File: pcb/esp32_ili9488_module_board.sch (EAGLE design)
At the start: 20 parts, among them U1 ILI9488 module, U2 ESP-WROOM/WROVER-32, U3 APK2112K-3.3TRG1, X1 HEADER-FTDI232, X2 USB-MICRO-B-FCI, X3 BOOT, X4 RESET, X5 QWIIC

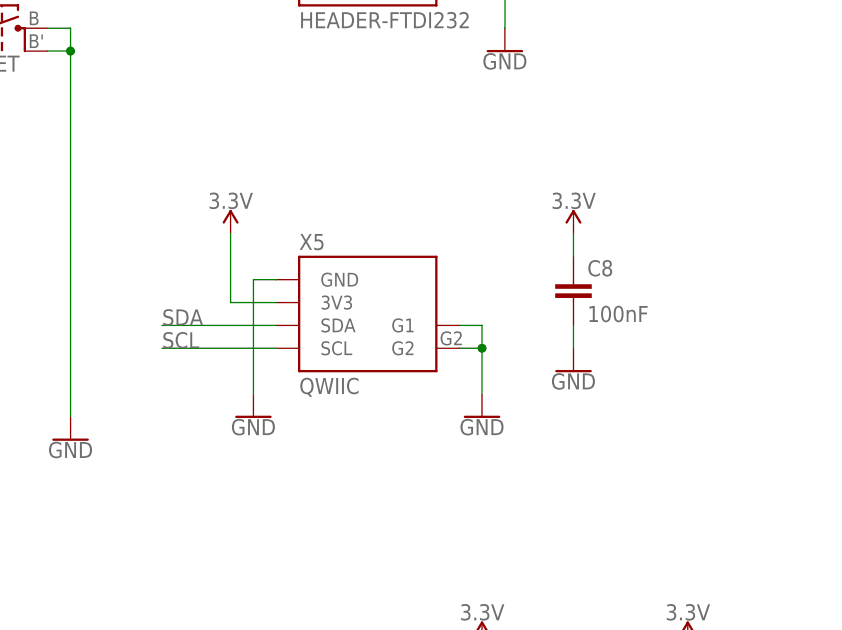
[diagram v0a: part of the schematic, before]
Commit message: Add I2C pullups
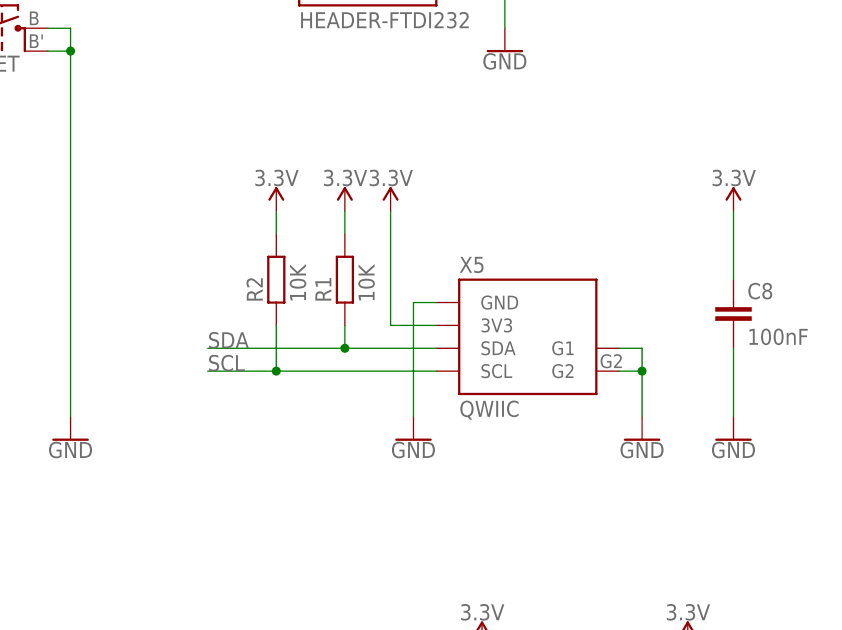
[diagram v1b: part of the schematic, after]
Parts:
- added R1, R2: 10K, M2M-Passives:RESISTOR0603
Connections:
- net 3.3V: now also R1.2, R2.2
- net SCL: now also R2.1
- net SDA: now also R1.1
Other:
- moved on the sheet: C8, X5
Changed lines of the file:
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@@
 <part name="SUPPLY13" library="M2M-Power" deviceset="3.3V" device=""/>
 <part name="GND20" library="M2M-Power" deviceset="GND" device=""/>
+<part name="R1" library="M2M-Passives" deviceset="RESISTOR" device="0603" value="10K"/>
+<part name="R2" library="M2M-Passives" deviceset="RESISTOR" device="0603" value="10K"/>
+<part name="SUPPLY14" library="M2M-Power" deviceset="3.3V" device=""/>
+<part name="SUPPLY15" library="M2M-Power" deviceset="3.3V" device=""/>
 </parts>
 <sheets>
@@
 <attribute name="VALUE" x="12.7" y="144.526" size="1.778" layer="96" align="top-center"/>
 </instance>
-<instance part="X5" gate="G$1" x="200.66" y="106.68" smashed="yes">
-<attribute name="NAME" x="193.04" y="115.062" size="1.778" layer="95"/>
-<attribute name="VALUE" x="193.04" y="99.06" size="1.778" layer="96"/>
-</instance>
-<instance part="GND17" gate="1" x="213.36" y="96.52" smashed="yes">
-<attribute name="VALUE" x="213.36" y="96.266" size="1.778" layer="96" align="top-center"/>
-</instance>
-<instance part="GND18" gate="1" x="187.96" y="96.52" smashed="yes">
-<attribute name="VALUE" x="187.96" y="96.266" size="1.778" layer="96" align="top-center"/>
-</instance>
-<instance part="SUPPLY11" gate="G$1" x="185.42" y="116.84" smashed="yes">
-<attribute name="VALUE" x="185.42" y="119.634" size="1.778" layer="96" align="bottom-center"/>
+<instance part="X5" gate="G$1" x="218.44" y="104.14" smashed="yes">
+<attribute name="NAME" x="210.82" y="112.522" size="1.778" layer="95"/>
+<attribute name="VALUE" x="210.82" y="96.52" size="1.778" layer="96"/>
+</instance>
+<instance part="GND17" gate="1" x="231.14" y="93.98" smashed="yes">
+<attribute name="VALUE" x="231.14" y="93.726" size="1.778" layer="96" align="top-center"/>
+</instance>
+<instance part="GND18" gate="1" x="205.74" y="93.98" smashed="yes">
+<attribute name="VALUE" x="205.74" y="93.726" size="1.778" layer="96" align="top-center"/>
+</instance>
+<instance part="SUPPLY11" gate="G$1" x="203.2" y="119.38" smashed="yes">
+<attribute name="VALUE" x="203.2" y="122.174" size="1.778" layer="96" align="bottom-center"/>
 </instance>
 <instance part="C7" gate="G$1" x="236.22" y="66.04" smashed="yes">
@@
 <attribute name="VALUE" x="236.22" y="55.626" size="1.778" layer="96" align="top-center"/>
 </instance>
-<instance part="C8" gate="G$1" x="223.52" y="111.76" smashed="yes">
-<attribute name="NAME" x="225.044" y="112.141" size="1.778" layer="95"/>
-<attribute name="VALUE" x="225.044" y="107.061" size="1.778" layer="96"/>
-</instance>
-<instance part="SUPPLY13" gate="G$1" x="223.52" y="116.84" smashed="yes">
-<attribute name="VALUE" x="223.52" y="119.634" size="1.778" layer="96" align="bottom-center"/>
-</instance>
-<instance part="GND20" gate="1" x="223.52" y="101.6" smashed="yes">
-<attribute name="VALUE" x="223.52" y="101.346" size="1.778" layer="96" align="top-center"/>
+<instance part="C8" gate="G$1" x="241.3" y="109.22" smashed="yes">
+<attribute name="NAME" x="242.824" y="109.601" size="1.778" layer="95"/>
+<attribute name="VALUE" x="242.824" y="104.521" size="1.778" layer="96"/>
+</instance>
+<instance part="SUPPLY13" gate="G$1" x="241.3" y="119.38" smashed="yes">
+<attribute name="VALUE" x="241.3" y="122.174" size="1.778" layer="96" align="bottom-center"/>
+</instance>
+<instance part="GND20" gate="1" x="241.3" y="93.98" smashed="yes">
+<attribute name="VALUE" x="241.3" y="93.726" size="1.778" layer="96" align="top-center"/>
+</instance>
+<instance part="R1" gate="G$1" x="198.12" y="111.76" smashed="yes" rot="R90">
+<attribute name="NAME" x="196.6214" y="109.22" size="1.778" layer="95" rot="R90"/>
+<attribute name="VALUE" x="201.422" y="109.22" size="1.778" layer="96" rot="R90"/>
+</instance>
+<instance part="R2" gate="G$1" x="190.5" y="111.76" smashed="yes" rot="R90">
+<attribute name="NAME" x="189.0014" y="109.22" size="1.778" layer="95" rot="R90"/>
+<attribute name="VALUE" x="193.802" y="109.22" size="1.778" layer="96" rot="R90"/>
+</instance>
+<instance part="SUPPLY14" gate="G$1" x="198.12" y="119.38" smashed="yes">
+<attribute name="VALUE" x="198.12" y="122.174" size="1.778" layer="96" align="bottom-center"/>
+</instance>
+<instance part="SUPPLY15" gate="G$1" x="190.5" y="119.38" smashed="yes">
+<attribute name="VALUE" x="190.5" y="122.174" size="1.778" layer="96" align="bottom-center"/>
 </instance>
 </instances>
@@
 <pinref part="GND18" gate="1" pin="GND"/>
 <pinref part="X5" gate="G$1" pin="GND"/>
-<wire x1="187.96" y1="99.06" x2="187.96" y2="111.76" width="0.1524" layer="91"/>
-<wire x1="187.96" y1="111.76" x2="190.5" y2="111.76" width="0.1524" layer="91"/>
+<wire x1="205.74" y1="96.52" x2="205.74" y2="109.22" width="0.1524" layer="91"/>
+<wire x1="205.74" y1="109.22" x2="208.28" y2="109.22" width="0.1524" layer="91"/>
 </segment>
 <segment>
 <pinref part="GND17" gate="1" pin="GND"/>
 <pinref part="X5" gate="G$1" pin="G1"/>
-<wire x1="213.36" y1="99.06" x2="213.36" y2="104.14" width="0.1524" layer="91"/>
-<wire x1="213.36" y1="104.14" x2="213.36" y2="106.68" width="0.1524" layer="91"/>
-<wire x1="213.36" y1="106.68" x2="210.82" y2="106.68" width="0.1524" layer="91"/>
+<wire x1="231.14" y1="96.52" x2="231.14" y2="101.6" width="0.1524" layer="91"/>
+<wire x1="231.14" y1="101.6" x2="231.14" y2="104.14" width="0.1524" layer="91"/>
+<wire x1="231.14" y1="104.14" x2="228.6" y2="104.14" width="0.1524" layer="91"/>
 <pinref part="X5" gate="G$1" pin="G2"/>
-<wire x1="210.82" y1="104.14" x2="213.36" y2="104.14" width="0.1524" layer="91"/>
-<junction x="213.36" y="104.14"/>
+<wire x1="228.6" y1="101.6" x2="231.14" y2="101.6" width="0.1524" layer="91"/>
+<junction x="231.14" y="101.6"/>
 </segment>
 <segment>
@@
 <pinref part="C8" gate="G$1" pin="2"/>
 <pinref part="GND20" gate="1" pin="GND"/>
-<wire x1="223.52" y1="106.68" x2="223.52" y2="104.14" width="0.1524" layer="91"/>
+<wire x1="241.3" y1="104.14" x2="241.3" y2="96.52" width="0.1524" layer="91"/>
 </segment>
 </net>
@@
 <segment>
 <pinref part="X5" gate="G$1" pin="3V3"/>
-<wire x1="190.5" y1="109.22" x2="185.42" y2="109.22" width="0.1524" layer="91"/>
+<wire x1="208.28" y1="106.68" x2="203.2" y2="106.68" width="0.1524" layer="91"/>
 <pinref part="SUPPLY11" gate="G$1" pin="3.3V"/>
-<wire x1="185.42" y1="109.22" x2="185.42" y2="116.84" width="0.1524" layer="91"/>
+<wire x1="203.2" y1="106.68" x2="203.2" y2="119.38" width="0.1524" layer="91"/>
 </segment>
 <segment>
@@
 <pinref part="SUPPLY13" gate="G$1" pin="3.3V"/>
 <pinref part="C8" gate="G$1" pin="1"/>
-<wire x1="223.52" y1="116.84" x2="223.52" y2="114.3" width="0.1524" layer="91"/>
+<wire x1="241.3" y1="119.38" x2="241.3" y2="111.76" width="0.1524" layer="91"/>
+</segment>
+<segment>
+<pinref part="SUPPLY15" gate="G$1" pin="3.3V"/>
+<pinref part="R2" gate="G$1" pin="2"/>
+<wire x1="190.5" y1="119.38" x2="190.5" y2="116.84" width="0.1524" layer="91"/>
+</segment>
+<segment>
+<pinref part="SUPPLY14" gate="G$1" pin="3.3V"/>
+<pinref part="R1" gate="G$1" pin="2"/>
+<wire x1="198.12" y1="119.38" x2="198.12" y2="116.84" width="0.1524" layer="91"/>
 </segment>
 </net>
@@
 <segment>
 <pinref part="X5" gate="G$1" pin="SDA"/>
-<wire x1="190.5" y1="106.68" x2="177.8" y2="106.68" width="0.1524" layer="91"/>
-<label x="177.8" y="106.68" size="1.778" layer="95"/>
+<wire x1="208.28" y1="104.14" x2="198.12" y2="104.14" width="0.1524" layer="91"/>
+<label x="182.88" y="104.14" size="1.778" layer="95"/>
+<pinref part="R1" gate="G$1" pin="1"/>
+<wire x1="198.12" y1="104.14" x2="182.88" y2="104.14" width="0.1524" layer="91"/>
+<wire x1="198.12" y1="106.68" x2="198.12" y2="104.14" width="0.1524" layer="91"/>
+<junction x="198.12" y="104.14"/>
 </segment>
 <segment>
@@
 <segment>
 <pinref part="X5" gate="G$1" pin="SCL"/>
-<wire x1="190.5" y1="104.14" x2="177.8" y2="104.14" width="0.1524" layer="91"/>
-<label x="177.8" y="104.14" size="1.778" layer="95"/>
-</segment>
-<segment>
+<wire x1="208.28" y1="101.6" x2="190.5" y2="101.6" width="0.1524" layer="91"/>
+<label x="182.88" y="101.6" size="1.778" layer="95"/>
+<pinref part="R2" gate="G$1" pin="1"/>
+<wire x1="190.5" y1="101.6" x2="182.88" y2="101.6" width="0.1524" layer="91"/>
+<wire x1="190.5" y1="106.68" x2="190.5" y2="101.6" width="0.1524" layer="91"/>
+<junction x="190.5" y="101.6"/>
+</segment>
+<segment>
